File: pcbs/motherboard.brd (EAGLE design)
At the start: 160 x 100 mm, 33 parts, among them U1 DRV8302DCAR, U2 TEENSY3.2, U3 PSOC5LP, U4 IRF7749L, U5 IRF7749L, U6 IRF7749L, U7\ IRF7749L, U8 IRF7749L, U9 IRF7749L

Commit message: Laid out single FET stage
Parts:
- added TP1, TP2, TP3, TP4, TP5, TP6, TP7, TP8: TEST-POINT3, SparkFun-Connectors:PAD.03X.03
- moved C7 290.9 mm to (133.6, 77.1), turned to 90 degrees
- moved C6 286.2 mm to (131.3, 91.8), turned to 180 degrees
- moved R7 286.2 mm to (138.4, 79.0), turned to 180 degrees
- moved C5 284.8 mm to (131.3, 94.8), turned to 180 degrees
- moved C8 279.5 mm to (133.6, 56.4), turned to 90 degrees
- moved R8 276.9 mm to (138.5, 58.3), turned to 180 degrees
- moved R14 266.9 mm to (92.7, 37.7), turned to 90 degrees
- moved C4 266.1 mm to (131.7, 70.9), turned to 180 degrees
- moved C3 264.8 mm to (131.7, 73.9), turned to 180 degrees
- moved R12 260.7 mm to (87.7, 37.7), turned to 90 degrees
- moved R13 259.9 mm to (90.2, 37.7), turned to 90 degrees
- moved RIGHT_HALL 259.1 mm to (95.2, 33.0), turned to 180 degrees
- moved R3 252.2 mm to (132.0, 68.7)
- moved R4 249.9 mm to (132.1, 60.7)
- moved R5 245.5 mm to (132.5, 48.0)
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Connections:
- net GH_A: now also TP1.P$1
- net GH_B: now also TP4.P$1
- net GH_C: now also TP7.P$1
- net GL_A: now also TP2.P$1
- net GL_B: now also TP5.P$1
- net GL_C: now also TP8.P$1
- net SL_A: now also TP3.P$1
- net SL_B: now also TP6.P$1
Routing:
- net VCC: track 0.00 -> 55.6 mm
- net +5V: track 0.00 -> 24.2 mm
- net SH_C: track 0.00 -> 18.5 mm
- net SH_A: track 0.00 -> 18.5 mm
- net SH_B: track 0.00 -> 18.5 mm
- net SL_A: track 0.00 -> 12.9 mm
- net SL_B: track 0.00 -> 10.9 mm
- net N$4: track 0.00 -> 8.35 mm
- net N$6: track 0.00 -> 7.91 mm
- net N$7: track 0.00 -> 7.61 mm
- net N$9: track 0.00 -> 7.56 mm
- net N$5: track 0.00 -> 7.54 mm
- net N$8: track 0.00 -> 7.48 mm
- net RIGHT_HALL_B: track 0.00 -> 3.86 mm
- net RIGHT_HALL_A: track 0.00 -> 3.86 mm
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- added copper zone on layer 1, net SH_A
- added copper zone on layer 1, net SH_B
- added copper zone on layer 1, net SH_C
- added copper zone on layer 1, net SL_A
- added copper zone on layer 1, net SL_B
- added copper zone on layer 1, net VCC

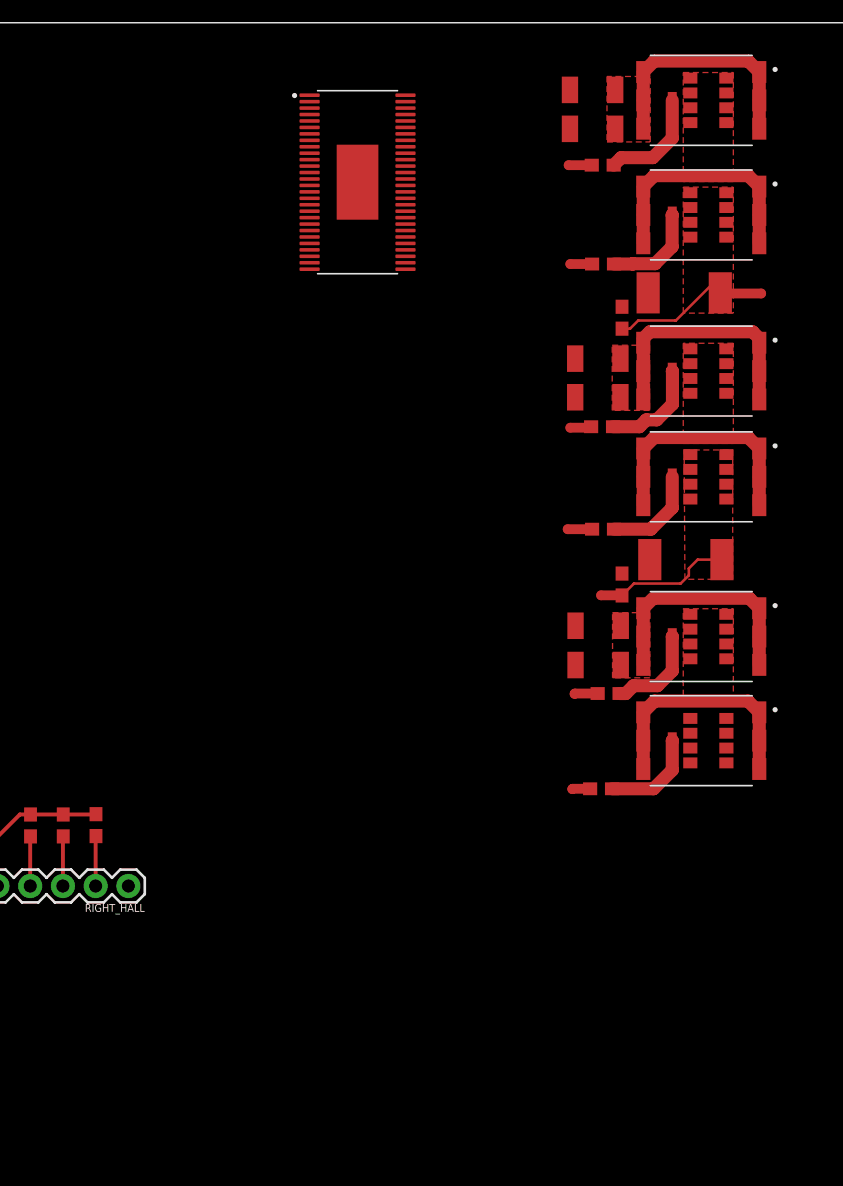
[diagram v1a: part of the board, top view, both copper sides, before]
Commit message: Cleaned up eagle directory, laid out more of power stage
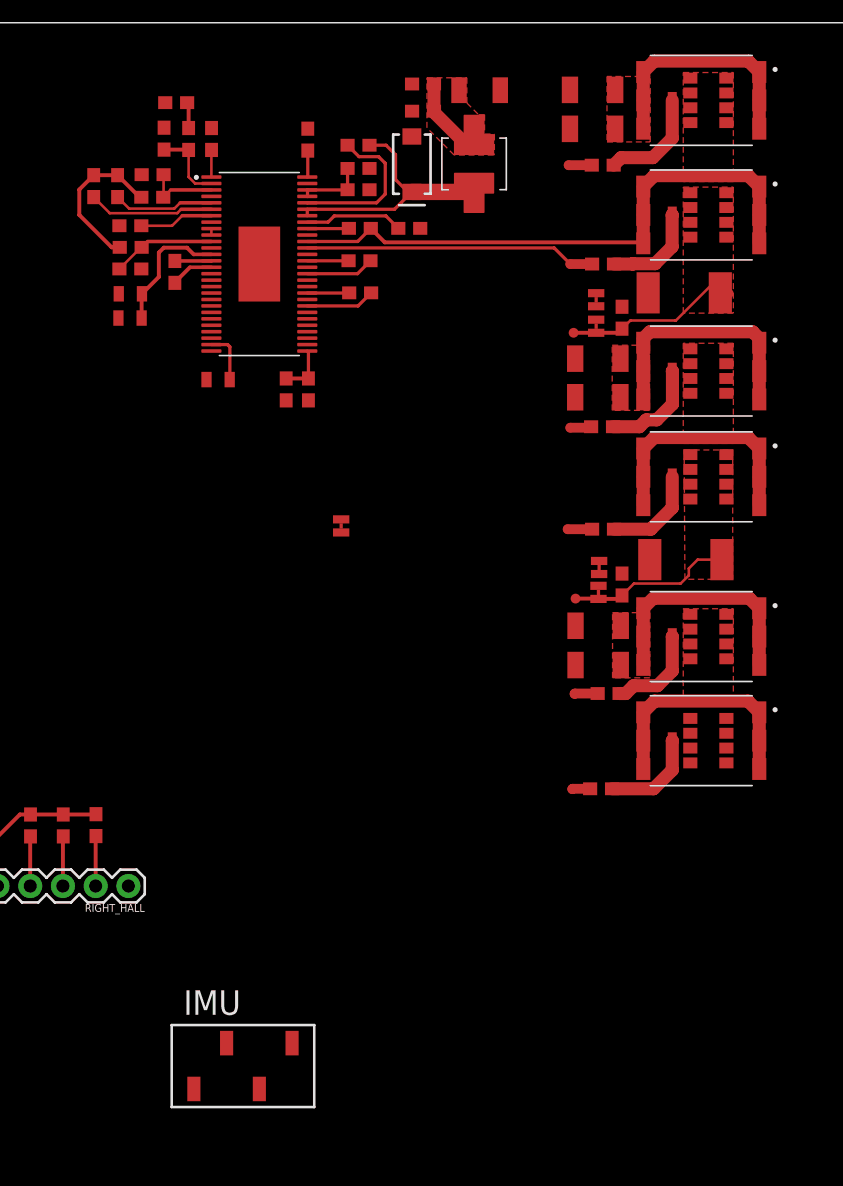
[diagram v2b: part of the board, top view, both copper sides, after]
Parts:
- added C10: 120pF, SparkFun-Capacitors:0603
- added C11, C12, C14: 2.2uF, SparkFun-Capacitors:0805
- added C13: 22nF 36V, SparkFun-Capacitors:0603
- added C15, C17, C23: 4.7uF, SparkFun-Capacitors:0603
- added C16, C18, C19, C20, C21, C22, C24: 0.1uF, SparkFun-Capacitors:0603
- added C25: 100uF, SparkFun-Retired:1210
- added C26: 15nF, SparkFun-Capacitors:0603
- added C9: 6.8nF, SparkFun-Capacitors:0603
- added D1: NRVBA2H100T3G, SparkFun-DiscreteSemi:SMA-DIODE
- added IMU: SSM-104-L-SV, kanzi:SAMTEC-SSM-104-X-SV
- added JP1, JP2, JP3, JP4, JP5: JUMPER-SMT_2_NC_TRACE_NO-SILK, SparkFun-Jumpers:SMT-JUMPER_2_NC_TRACE_NO-SILK
- added L1: 22uH, IndividualNode:LQH43
- added R15: 200k, SparkFun-Resistors:0603
- added R16: 16.2k, SparkFun-Resistors:0603
- added R17, R18, R19, R20, R21: 10k, SparkFun-Resistors:0603
- added R22: OPEN, SparkFun-Resistors:0603
- added R23: SHORT, SparkFun-Resistors:0603
- added R24: 1M, SparkFun-Resistors:0603
- moved TP3 14.9 mm to (129.8, 75.9)
- moved U1 9.92 mm to (105.4, 81.3)
- moved TP6 2.00 mm to (129.9, 55.3)
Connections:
- removed net AVDD: U1.27
- removed net BST_A: U1.48
- removed net BST_B: U1.43
- removed net BST_BK: U1.52
- removed net BST_C: U1.38
- removed net CP1: U1.14
- removed net CP2: U1.15
- removed net DVDD: U1.23
- removed net GVDD: U1.13
- removed net PVDD1: U1.29
- removed net PVDD2: U1.53, U1.54
- removed net PWR_PAD: U1.57
- new net +3V3: IMU.3, U2.26
- new net ENABLE: U1.16, U2.15
- new net LEFT_DC_CAL: U1.12
- new net LEFT_FAULT: R19.1, U1.6, U2.24
- new net LEFT_OCTW: R20.1, U1.5, U2.25
- new net LEFT_SO1: U1.25, U2.19
- new net LEFT_SO2: U1.26, U2.18
- new net N$1: R15.1, U1.1
- new net N$10: R17.2, R18.1, U1.3
- new net N$11: R22.1, R23.2, U1.11
- new net N$12: C11.1, C12.1, U1.13
- new net N$13: R21.2, U1.7
- new net N$14: R23.1, U1.23
- new net N$15: C13.1, U1.14
- new net N$16: C13.2, U1.15
- new net N$17: C14.1, U1.27
- new net N$18: C15.1, C16.1, U1.29
- new net N$19: C17.1, C18.1, U1.53, U1.54
- new net N$2: C9.2, R16.2
- new net N$20: C19.2, U1.38
- new net N$21: C20.2, U1.43
- new net N$22: C21.2, U1.48
- new net N$23: R24.1, U1.49
- new net N$24: C22.2, U1.52
- new net N$25: C22.1, D1.C, L1.1, U1.50, U1.51
- new net N$26: C23.1, C24.1, C25.1, L1.2
- new net N$27: C26.2, U1.56
- new net N$3: C10.2, R16.1, U1.2
- new net RIGHT_FAULT: U2.22
- new net RIGHT_OCTW: U2.23
- new net RIGHT_SO1: U2.17
- new net RIGHT_SO2: U2.16
- new net SCL: IMU.1, U2.21
- new net SDA: IMU.2, U2.20
- net +5V: now also R18.2, R19.2, R20.2, R22.2, U1.10, U1.24, U1.9, U2.28
- net AGND: now also JP2.2, JP4.2, JP5.2; no longer U1.28
- net DGND: now also C10.1, C11.2, C12.2, C14.2, C15.2, C16.2, C17.2, C18.2, C23.2, C24.2, C25.2, C26.1, C9.1, D1.A, IMU.4, R15.2, R17.1, R21.1, R24.2, U1.28, U1.57, U1.8
- net LEFT_DIR: now also U2.9
- net LEFT_PWM: now also U2.7
- net RIGHT_DIR: now also U2.10
- net RIGHT_PWM: now also U2.8
- net SH_A: now also C21.1
- net SH_B: now also C20.1
- net SH_C: now also C19.1
- net SL_A: now also JP1.2
- net SL_B: now also JP3.2
- net SL_C: now also JP5.1
- net SN1: now also JP1.1
- net SN2: now also JP3.1
- net SP1: now also JP2.1
- net SP2: now also JP4.1
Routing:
- net SH_A: track 18.5 -> 45.5 mm
- net GL_A: track 1.69 -> 22.6 mm
- net N$25: track 0.00 -> 20.2 mm
- net +5V: track 24.2 -> 36.9 mm
- net N$24: track 0.00 -> 12.2 mm
- net N$12: track 0.00 -> 10.1 mm
- net LEFT_FAULT: track 0.00 -> 9.78 mm
- net N$11: track 0.00 -> 8.13 mm
- net LEFT_OCTW: track 0.00 -> 7.83 mm
- net N$23: track 0.00 -> 7.66 mm
- net N$26: track 0.00 -> 6.34 mm
- net N$3: track 0.00 -> 5.99 mm
- net N$13: track 0.00 -> 5.95 mm
- net N$10: track 0.00 -> 5.90 mm
- net SH_C: track 18.5 -> 23.9 mm
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- added copper zone on layer 1, net N$26

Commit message: Finished first motor channel
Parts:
- moved JP5 28.2 mm to (133.2, 42.6)
- moved C20 9.41 mm to (122.6, 82.0), turned to 90 degrees
- moved C19 5.37 mm to (118.5, 80.3)
- moved C11 2.84 mm to (97.9, 80.2)
- moved C25 2.84 mm to (125.0, 96.0)
- moved R19 2.84 mm to (95.1, 88.6)
- moved R20 2.84 mm to (97.0, 88.6)
- moved R24 2.84 mm to (119.6, 85.3)
- moved C12 2.84 mm to (97.9, 78.4)
- moved C14 2.84 mm to (104.7, 73.6)
- moved C16 2.84 mm to (111.8, 72.8)
- moved C23 2.84 mm to (120.7, 94.4)
- moved C24 2.84 mm to (120.7, 96.5)
- moved C9 2.84 mm to (101.5, 95.1)
- moved D1 2.84 mm to (119.8, 90.3)
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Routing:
- net GL_C: track 1.40 -> 53.0 mm, vias 0 -> 2
- net SL_C: track 0.00 -> 50.5 mm, vias 0 -> 2
- net GH_C: track 1.80 -> 47.9 mm, vias 0 -> 2
- net SH_C: track 23.9 -> 62.3 mm, vias 0 -> 2
- net SL_B: track 12.9 -> 51.2 mm, vias 0 -> 2
- net SP2: track 0.00 -> 35.8 mm
- net SN2: track 0.00 -> 34.6 mm
- net GL_B: track 1.89 -> 35.4 mm, vias 0 -> 2
- net GH_B: track 1.65 -> 28.7 mm, vias 0 -> 2
- net SH_B: track 23.8 -> 48.9 mm, vias 0 -> 2
- net SL_A: track 14.3 -> 36.0 mm, vias 0 -> 2
- net SN1: track 0.00 -> 20.6 mm
- net SP1: track 0.00 -> 20.0 mm
- net GH_A: track 1.79 -> 21.3 mm, vias 0 -> 2
- net N$21: track 3.20 -> 11.4 mm
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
